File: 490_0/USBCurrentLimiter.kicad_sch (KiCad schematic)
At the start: 18 parts, among them U2 TPS2553DBVR, U3 TPS2553DBVR

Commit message: Footprint Update
1st half of footprints updated
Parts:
- D1, D2: footprint (none) -> LED_SMD:LED_0805_2012Metric
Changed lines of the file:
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@@
 			)
 		)
-		(property "Footprint" ""
+		(property "Footprint" "LED_SMD:LED_0805_2012Metric"
 			(at 156.21 104.14 0)
 			(effects
@@
 			)
 		)
-		(property "Footprint" ""
+		(property "Footprint" "LED_SMD:LED_0805_2012Metric"
 			(at 156.21 60.96 0)
 			(effects

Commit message: Footprint Update #2
All footprints except for the capacitors have been attributed
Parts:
- R3, R39, R40, R5: footprint (none) -> Resistor_SMD:R_0603_1608Metric
- U2, U3: footprint TPS2553DBVR:SOT95P280X145-6N -> *CapStone*:SOT95P280X145-6N_TPS2553DBVR
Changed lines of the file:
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@@
 			)
 		)
-		(property "Footprint" "TPS2553DBVR:SOT95P280X145-6N"
+		(property "Footprint" "*CapStone*:SOT95P280X145-6N_TPS2553DBVR"
 			(at 127 121.92 0)
 			(effects
@@
 			)
 		)
-		(property "Footprint" ""
+		(property "Footprint" "Resistor_SMD:R_0603_1608Metric"
 			(at 100.33 76.962 90)
 			(effects
@@
 			)
 		)
-		(property "Footprint" "TPS2553DBVR:SOT95P280X145-6N"
+		(property "Footprint" "*CapStone*:SOT95P280X145-6N_TPS2553DBVR"
 			(at 127 78.74 0)
 			(effects
@@
 			)
 		)
-		(property "Footprint" ""
+		(property "Footprint" "Resistor_SMD:R_0603_1608Metric"
 			(at 163.83 62.738 90)
 			(effects
@@
 			)
 		)
-		(property "Footprint" ""
+		(property "Footprint" "Resistor_SMD:R_0603_1608Metric"
 			(at 100.33 120.142 90)
 			(effects
@@
 			)
 		)
-		(property "Footprint" ""
+		(property "Footprint" "Resistor_SMD:R_0603_1608Metric"
 			(at 163.83 105.918 90)
 			(effects

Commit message: March 3rd
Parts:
- C11, C3, C63, C64: value 0.1u -> 100n; footprint (none) -> Capacitor_SMD:C_0603_1608Metric; Digikey Link https://www.digikey.ca/en/products/detail/yageo/CC0805JRX7R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 -> https://www.digikey.ca/en/products/detail/yageo/CC0603KRX7R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; Manufacturer Part CC0805JRX7R7BB104 -> CC0603KRX7R9BB104; Package 0805 -> 0603 (1608 Metric); Price 0.11 -> 0.08; Supplier P/N 311-4266-1-ND -> 311-1344-1-ND
- C12, C4: footprint (none) -> Capacitor_SMD:C_0805_2012Metric; Digikey Link https://www.digikey.ca/en/products/detail/kemet/c1206c106k4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 -> https://www.digikey.ca/en/products/detail/samsung-electro-m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; Manufacturer KEMET -> Samsung Electro-Mechanics; Manufacturer Part C1206C106K4RACTU -> CL21B106KOQNNNE; Package 1206 (3216 Metric) -> 0805; Price 0.31 -> 0.22; Supplier P/N 399-C1206C106K4RACTUCT-ND -> 1276-2872-1-ND
- C16, C8: footprint (none) -> Capacitor_Tantalum_SMD:CP_EIA-7260-38_AVX-R_HandSolder; Digikey Link https://www.digikey.ca/en/products/detail/vishay-sprague/29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 -> https://www.digikey.ca/en/products/detail/vishay-sprague/59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; Manufacturer Part 293D127X96R3D2TE3 -> 594D127X9020R2T; Package 2917 (7343 Metric) -> 2824 (7260 Metric); Price 0.99 -> 6.97; Supplier P/N 718-1745-1-ND -> 718-594D127X9020R2TCT-ND
- D1, D2: value LED -> LTST-C170TBKT
- R3, R5: footprint Resistor_SMD:R_0603_1608Metric -> Resistor_SMD:R_0805_2012Metric; Digikey Link https://www.digikey.ca/en/products/detail/yageo/RC1206FR-07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 -> https://www.digikey.ca/en/products/detail/yageo/RC0805FR-07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; Manufacturer Part RC1206FR-071KL -> RC0805FR-071KL; Package 1206 -> 0805; Price 0.11 -> 0.1; Supplier P/N 311-1.00KFRCT-ND -> 311-1.00KCRCT-ND
- R39, R40: value 100K -> 100k; footprint Resistor_SMD:R_0603_1608Metric -> Resistor_SMD:R_0805_2012Metric; Digikey Link https://www.digikey.ca/en/products/detail/yageo/RC1206FR-07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 -> https://www.digikey.ca/en/products/detail/yageo/RC0805FR-07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; Manufacturer Part RC1206FR-07100KL -> RC0805FR-07100KL; Package 1206 -> 0805; Supplier P/N 311-100KFRCT-ND -> 311-100KCRCT-ND
- R4, R6: footprint Resistor_THT:R_Axial_DIN0207_L6.3mm_D2.5mm_P10.16mm_Horizontal -> Resistor_SMD:R_0805_2012Metric

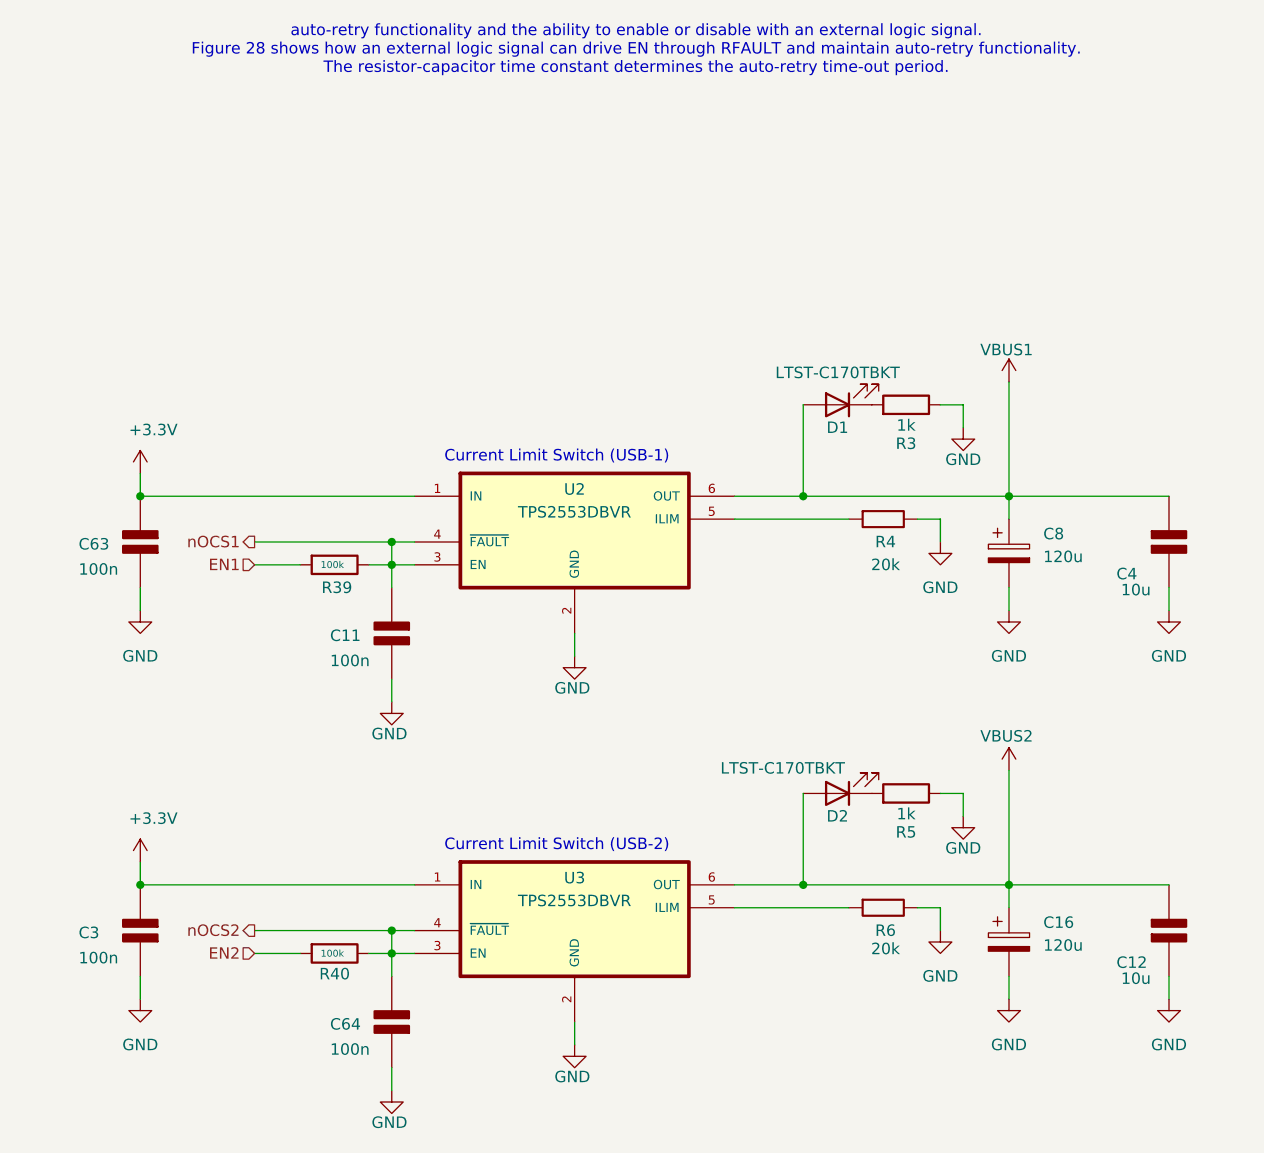
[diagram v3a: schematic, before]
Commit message: changed power and ground symbols for glasses
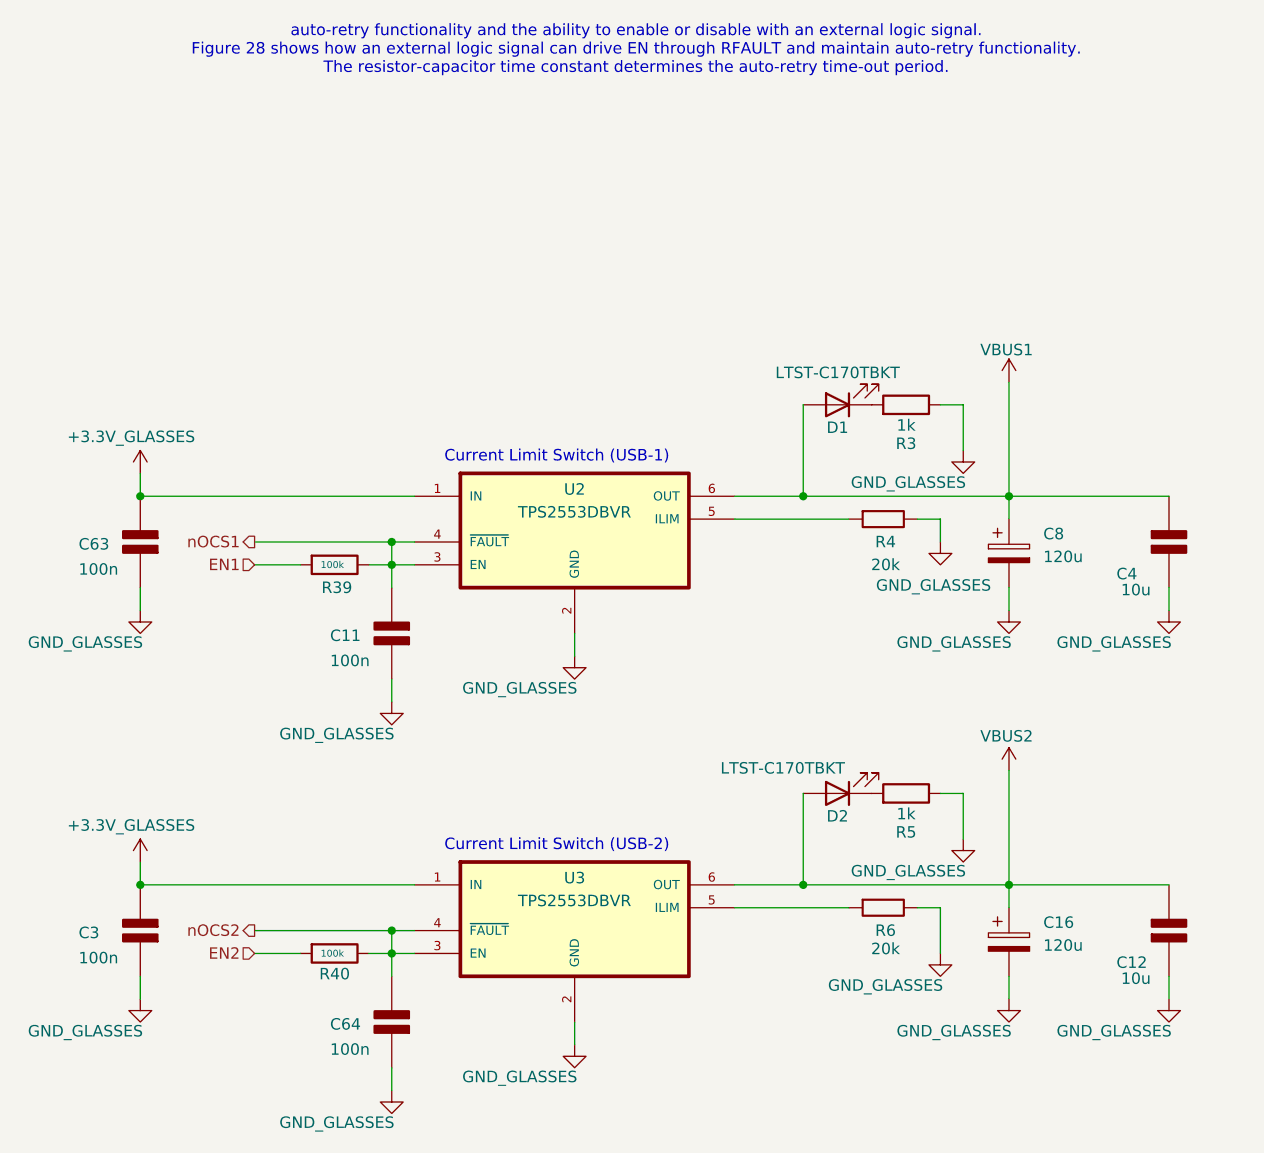
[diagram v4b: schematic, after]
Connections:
- net +3.3V renamed +3.3V_GLASSES
- net GND renamed GND_GLASSES

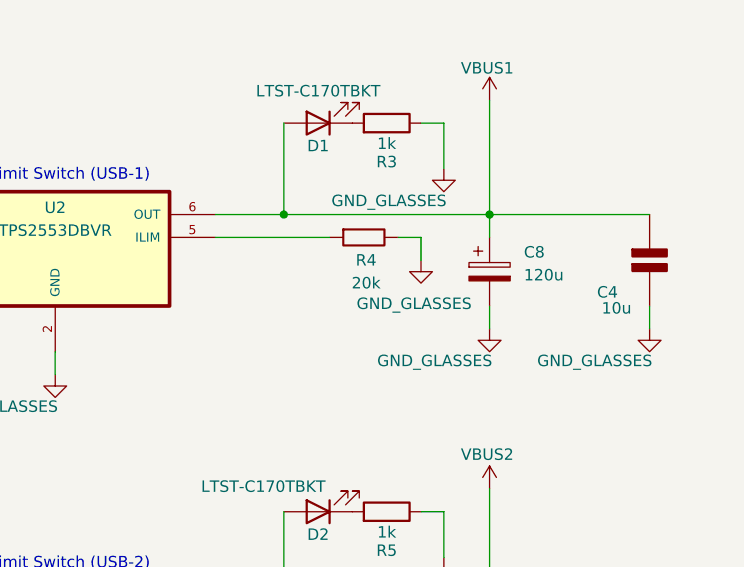
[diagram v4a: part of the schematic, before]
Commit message: ERC check fix
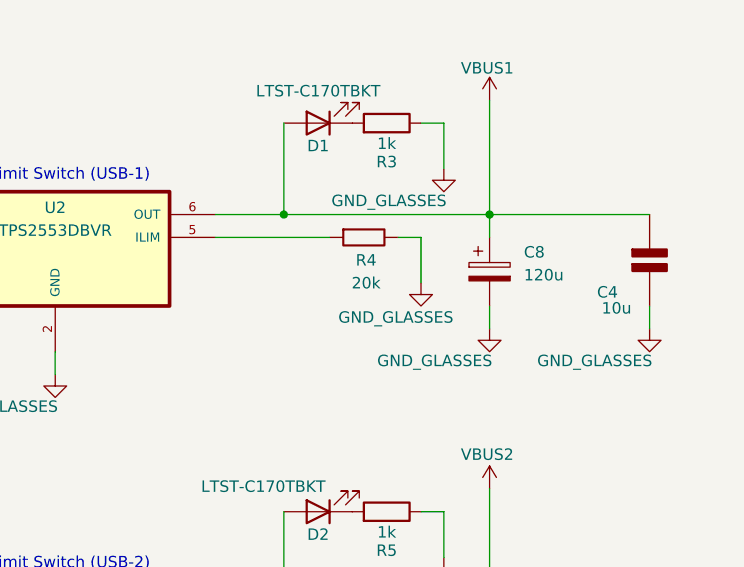
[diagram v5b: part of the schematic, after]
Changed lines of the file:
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@@
 	(wire
 		(pts
-			(xy 167.64 76.2) (xy 167.64 73.66)
+			(xy 167.64 78.74) (xy 167.64 73.66)
 		)
 		(stroke
@@
 	(symbol
 		(lib_id "power:GND")
-		(at 167.64 76.2 0)
+		(at 167.64 78.74 0)
 		(unit 1)
 		(exclude_from_sim no)
@@
 		(dnp no)
 		(property "Reference" "#PWR010"
-			(at 167.64 82.55 0)
+			(at 167.64 85.09 0)
 			(effects
 				(font
@@
 		)
 		(property "Value" "GND_GLASSES"
-			(at 166.878 81.026 0)
+			(at 164.846 82.55 0)
 			(effects
 				(font
@@
 		)
 		(property "Footprint" ""
-			(at 167.64 76.2 0)
+			(at 167.64 78.74 0)
 			(effects
 				(font
@@
 		)
 		(property "Datasheet" ""
-			(at 167.64 76.2 0)
+			(at 167.64 78.74 0)
 			(effects
 				(font
@@
 		)
 		(property "Description" "Power symbol creates a global label with name \"GND\" , ground"
-			(at 167.64 76.2 0)
+			(at 167.64 78.74 0)
 			(effects
 				(font

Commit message: Added side B for SW1
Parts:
- C11, C12, C3, C4, C63, C64: symbol PCM_Elektuur:C -> capstone_parts:C
- C16, C8: symbol Device:C_Polarized -> capstone_parts:C_Polarized
- D1, D2: symbol Device:LED -> capstone_parts:LED
- R3, R39, R40, R5: symbol Device:R -> capstone_parts:R
- R4, R6: symbol PCM_SL_Resistors:Resistor -> capstone_parts:Resistor
- U2: symbol capstone_parts:TPS2553DBVR -> capstone_parts:TPS2553DBVR_2
- U3: symbol capstone_parts:TPS2553DBVR -> capstone_parts:TPS2553DBVR_1
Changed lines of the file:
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@@
 	)
 	(symbol
-		(lib_id "PCM_Elektuur:C")
+		(lib_id "capstone_parts:C")
 		(at 78.74 76.2 180)
 		(unit 1)
@@
 	(symbol
 		(lib_name "TPS2553DBVR_1")
-		(lib_id "capstone_parts:TPS2553DBVR")
+		(lib_id "capstone_parts:TPS2553DBVR_1")
 		(at 127 121.92 0)
 		(unit 1)
@@
 	)
 	(symbol
-		(lib_id "Device:R")
+		(lib_id "capstone_parts:R")
 		(at 100.33 78.74 270)
 		(unit 1)
@@
 	)
 	(symbol
-		(lib_id "PCM_Elektuur:C")
+		(lib_id "capstone_parts:C")
 		(at 106.68 129.54 180)
 		(unit 1)
@@
 	)
 	(symbol
-		(lib_id "PCM_Elektuur:C")
+		(lib_id "capstone_parts:C")
 		(at 193.04 76.2 0)
 		(unit 1)
@@
 	)
 	(symbol
-		(lib_id "Device:C_Polarized")
+		(lib_id "capstone_parts:C_Polarized")
 		(at 175.26 120.65 0)
 		(unit 1)
@@
 	)
 	(symbol
-		(lib_id "Device:LED")
+		(lib_id "capstone_parts:LED")
 		(at 156.21 104.14 180)
 		(unit 1)
@@
 	)
 	(symbol
-		(lib_id "PCM_SL_Resistors:Resistor")
+		(lib_id "capstone_parts:Resistor")
 		(at 161.29 116.84 0)
 		(unit 1)
@@
 	)
 	(symbol
-		(lib_id "PCM_SL_Resistors:Resistor")
+		(lib_id "capstone_parts:Resistor")
 		(at 161.29 73.66 0)
 		(unit 1)
@@
 	(symbol
 		(lib_name "TPS2553DBVR_2")
-		(lib_id "capstone_parts:TPS2553DBVR")
+		(lib_id "capstone_parts:TPS2553DBVR_2")
 		(at 127 78.74 0)
 		(unit 1)
@@
 	)
 	(symbol
-		(lib_id "PCM_Elektuur:C")
+		(lib_id "capstone_parts:C")
 		(at 106.68 86.36 180)
 		(unit 1)
@@
 	)
 	(symbol
-		(lib_id "PCM_Elektuur:C")
+		(lib_id "capstone_parts:C")
 		(at 193.04 119.38 0)
 		(unit 1)
@@
 	)
 	(symbol
-		(lib_id "Device:C_Polarized")
+		(lib_id "capstone_parts:C_Polarized")
 		(at 175.26 77.47 0)
 		(unit 1)
@@
 	)
 	(symbol
-		(lib_id "Device:R")
+		(lib_id "capstone_parts:R")
 		(at 163.83 60.96 270)
 		(mirror x)
@@
 	)
 	(symbol
-		(lib_id "Device:R")
+		(lib_id "capstone_parts:R")
 		(at 100.33 121.92 270)
 		(unit 1)
@@
 	)
 	(symbol
-		(lib_id "Device:LED")
+		(lib_id "capstone_parts:LED")
 		(at 156.21 60.96 180)
 		(unit 1)
@@
 	)
 	(symbol
-		(lib_id "Device:R")
+		(lib_id "capstone_parts:R")
 		(at 163.83 104.14 270)
 		(mirror x)
@@
 	)
 	(symbol
-		(lib_id "PCM_Elektuur:C")
+		(lib_id "capstone_parts:C")
 		(at 78.74 119.38 180)
 		(unit 1)

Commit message: Friday, March 20th: PCB Final for BOM
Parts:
- U2, U3: footprint *CapStone*:SOT95P280X145-6N_TPS2553DBVR -> capstone:SOT95P280X145-6N_TPS2553DBVR
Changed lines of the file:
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@@
 			)
 		)
+		(property "OPTION" ""
+			(at 78.74 76.2 0)
+			(effects
+				(font
+					(size 1.27 1.27)
+				)
+				(hide yes)
+			)
+		)
 		(pin "1"
 		)
@@
 			)
 		)
-		(property "Footprint" "*CapStone*:SOT95P280X145-6N_TPS2553DBVR"
+		(property "Footprint" "capstone:SOT95P280X145-6N_TPS2553DBVR"
 			(at 127 121.92 0)
 			(effects
@@
 			)
 		)
+		(property "OPTION" ""
+			(at 127 121.92 0)
+			(effects
+				(font
+					(size 1.27 1.27)
+				)
+				(hide yes)
+			)
+		)
 		(pin "5"
 		)
@@
 			)
 		)
+		(property "OPTION" ""
+			(at 100.33 78.74 90)
+			(effects
+				(font
+					(size 1.27 1.27)
+				)
+				(hide yes)
+			)
+		)
 		(pin "2"
 		)
@@
 			)
 		)
+		(property "OPTION" ""
+			(at 106.68 129.54 0)
+			(effects
+				(font
+					(size 1.27 1.27)
+				)
+				(hide yes)
+			)
+		)
 		(pin "1"
 		)
@@
 			)
 		)
+		(property "OPTION" ""
+			(at 193.04 76.2 0)
+			(effects
+				(font
+					(size 1.27 1.27)
+				)
+				(hide yes)
+			)
+		)
 		(pin "2"
 		)
@@
 			)
 		)
+		(property "OPTION" ""
+			(at 175.26 120.65 0)
+			(effects
+				(font
+					(size 1.27 1.27)
+				)
+				(hide yes)
+			)
+		)
 		(pin "1"
 		)
@@
 			)
 		)
+		(property "OPTION" ""
+			(at 156.21 104.14 0)
+			(effects
+				(font
+					(size 1.27 1.27)
+				)
+				(hide yes)
+			)
+		)
 		(pin "2"
 		)
@@
 			)
 		)
+		(property "OPTION" ""
+			(at 161.29 116.84 0)
+			(effects
+				(font
+					(size 1.27 1.27)
+				)
+				(hide yes)
+			)
+		)
 		(pin "1"
 		)
@@
 			)
 		)
+		(property "OPTION" ""
+			(at 161.29 73.66 0)
+			(effects
+				(font
+					(size 1.27 1.27)
+				)
+				(hide yes)
+			)
+		)
 		(pin "1"
 		)
@@
 			)
 		)
-		(property "Footprint" "*CapStone*:SOT95P280X145-6N_TPS2553DBVR"
+		(property "Footprint" "capstone:SOT95P280X145-6N_TPS2553DBVR"
 			(at 127 78.74 0)
 			(effects
@@
 			)
 		)
+		(property "OPTION" ""
+			(at 127 78.74 0)
+			(effects
+				(font
+					(size 1.27 1.27)
+				)
+				(hide yes)
+			)
+		)
 		(pin "5"
 		)
@@
 			)
 		)
+		(property "OPTION" ""
+			(at 106.68 86.36 0)
+			(effects
+				(font
+					(size 1.27 1.27)
+				)
+				(hide yes)
+			)
+		)
 		(pin "1"
 		)
@@
 			)
 		)
+		(property "OPTION" ""
+			(at 193.04 119.38 0)
+			(effects
+				(font
+					(size 1.27 1.27)
+				)
+				(hide yes)
+			)
+		)
 		(pin "2"
 		)
@@
 			)
 		)
+		(property "OPTION" ""
+			(at 175.26 77.47 0)
+			(effects
+				(font
+					(size 1.27 1.27)
+				)
+				(hide yes)
+			)
+		)
 		(pin "1"
 		)
@@
 			)
 		)
+		(property "OPTION" ""
+			(at 163.83 60.96 90)
+			(effects
+				(font
+					(size 1.27 1.27)
+				)
+				(hide yes)
+			)
+		)
 		(pin "1"
 		)
@@
 			)
 		)
+		(property "OPTION" ""
+			(at 100.33 121.92 90)
+			(effects
+				(font
+					(size 1.27 1.27)
+				)
+				(hide yes)
+			)
+		)
 		(pin "2"
 		)
@@
 			)
 		)
+		(property "OPTION" ""
+			(at 156.21 60.96 0)
+			(effects
+				(font
+					(size 1.27 1.27)
+				)
+				(hide yes)
+			)
+		)
 		(pin "2"
 		)
@@
 			)
 		)
+		(property "OPTION" ""
+			(at 163.83 104.14 90)
+			(effects
+				(font
+					(size 1.27 1.27)
+				)
+				(hide yes)
+			)
+		)
 		(pin "1"
 		)
@@
 			(at 78.74 119.38 0)
 			(effects
+				(font
+					(size 1.27 1.27)
+				)
+				(hide yes)
+			)
+		)
+		(property "OPTION" ""
+			(at 78.74 119.38 0)
+			(effects
